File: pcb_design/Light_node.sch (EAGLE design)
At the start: 42 parts, among them CN3 JSTPH, IC1 ATmega328P, IC2 MIC5225-3.3v, U1 MCP73831T-2ACI/OT, U2 LIS3DHTR, Y1 12MHz

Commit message: most of the layour is completed using standard LEDs, but we should move to neopixels on board
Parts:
- removed B2: red, microbuilder:LED0805_NOOUTLINE
- removed C6: 0.1uF, microbuilder:CAP_CERAMIC0805_10MGAP
- removed D2: SCHOTTKY, adafruit:DIODE_SOD-123FL
- removed JP1, JP4: (no value), adafruit:PINHD-1X12-CB
- removed JP6: (no value), microbuilder:HEADER-1X3ROUND
- removed R10: 470 (0603), microbuilder:RESISTOR_0603_NOOUT
- removed U$1, U$6: FIDUCIAL, adafruit:FIDUCIAL
- added CH_LED: GREEN, microbuilder:LED0805_NOOUTLINE
- added LED1: RGB_LED, 0_Shibbs1:RGB_LED
- added LED3, LED4: WS2812B5050, microbuilder:WS2812B5050
- added R13, R14, R15, R17, R18, R9: 470 (0603), microbuilder:RESISTOR_0603_NOOUT
- JP2: device microbuilder:HEADER-1X870MIL -> adafruit:PINHD-1X12-CB
- LED2: value GREEN -> RGB_LED; device microbuilder:LED0805_NOOUTLINE -> 0_Shibbs1:RGB_LED
- renumbered PWR to PWR_LED
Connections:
- removed net VBUS: FTDI.3, JP1.3
- removed net VIN: JP2.1
- new net +5V1: LED3.VDD, LED4.VDD
- new net GND1: LED3.GND, LED4.GND
- new net LED_CNTRL: LED3.DI
- new net N$10: LED2B_LED.-, R14.2
- new net N$11: LED1R_LED.-, R15.2
- new net N$12: LED1G_LED.-, R17.2
- new net N$13: LED1B_LED.-, R18.2
- new net N$14: LED2R_LED.-, R9.2
- new net N$15: LED4.DO
- net +3V3: no longer JP1.4
- net +5V: now also C1.1, D3.C, FTDI.3, IC2.EN, IC2.VIN; no longer D2.A, R10.2
- net 3.3V: no longer C6.1, JP2.2
- net A0: no longer JP4.7
- net A1: no longer JP4.8
- net A2: no longer JP4.9
- net A3: no longer JP4.10
- net A6: no longer R7.WIPER
- net A7: now also R7.WIPER
- net ADC1: no longer JP6.1
- net ADC2: no longer JP6.2
- net ADC3: no longer JP6.3
- net AREF: no longer JP4.6
- net CS: no longer JP2.7
- net D10: now also R9.1; no longer JP4.2
- net D11: now also R13.1; no longer JP4.3
- net D12: now also R14.1; no longer JP4.4
- net D13: no longer JP4.5
- net D2: now also R15.1
- net D3: now also R17.1; no longer JP1.9
- net D4: now also R18.1; no longer JP1.8
- net D5: no longer JP1.7
- net D6: no longer JP1.6
- net D8: no longer JP1.5
- net D9: no longer JP4.1
- net GND: now also CH_LED.C; no longer B2.C, C6.2, JP1.2, JP2.3, LED2.C
- net INT1: no longer JP2.8
- net N$4: now also LED3.DO, LED4.DI; no longer B2.A, R10.1
- net N$7: now also LED2G_LED.-, R13.2; no longer C1.1, D2.C, D3.C, IC2.EN, IC2.VIN
- net N$9: now also CH_LED.A; no longer LED2.A
- net RESET: no longer JP1.12
- net RXD: no longer JP1.11
- net SCL: no longer JP2.4, JP4.12
- net SDA: no longer JP2.5, JP4.11
- net SDO: no longer JP2.6
- net TXD: no longer JP1.10
- net VBAT: now also LED1B_LED.+, LED1G_LED.+, LED1R_LED.+, LED2B_LED.+, LED2G_LED.+, LED2R_LED.+; no longer JP1.1
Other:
- note added: "For USB-powered Designs : Short JP5 and DNP the lithium battery. If you don't do this things are going to get fucked up"
- note removed: "SDA (Pin 6) = Data In (MOSI)"
- note removed: "SDO (Pin 7) = Data Out (MISO)"
- note removed: "SPI"
- note removed: "Set SJ1 to make I2C"
- note removed: "address LSB 1"
- moved on the sheet: C7, CN1, R16, R8, U2

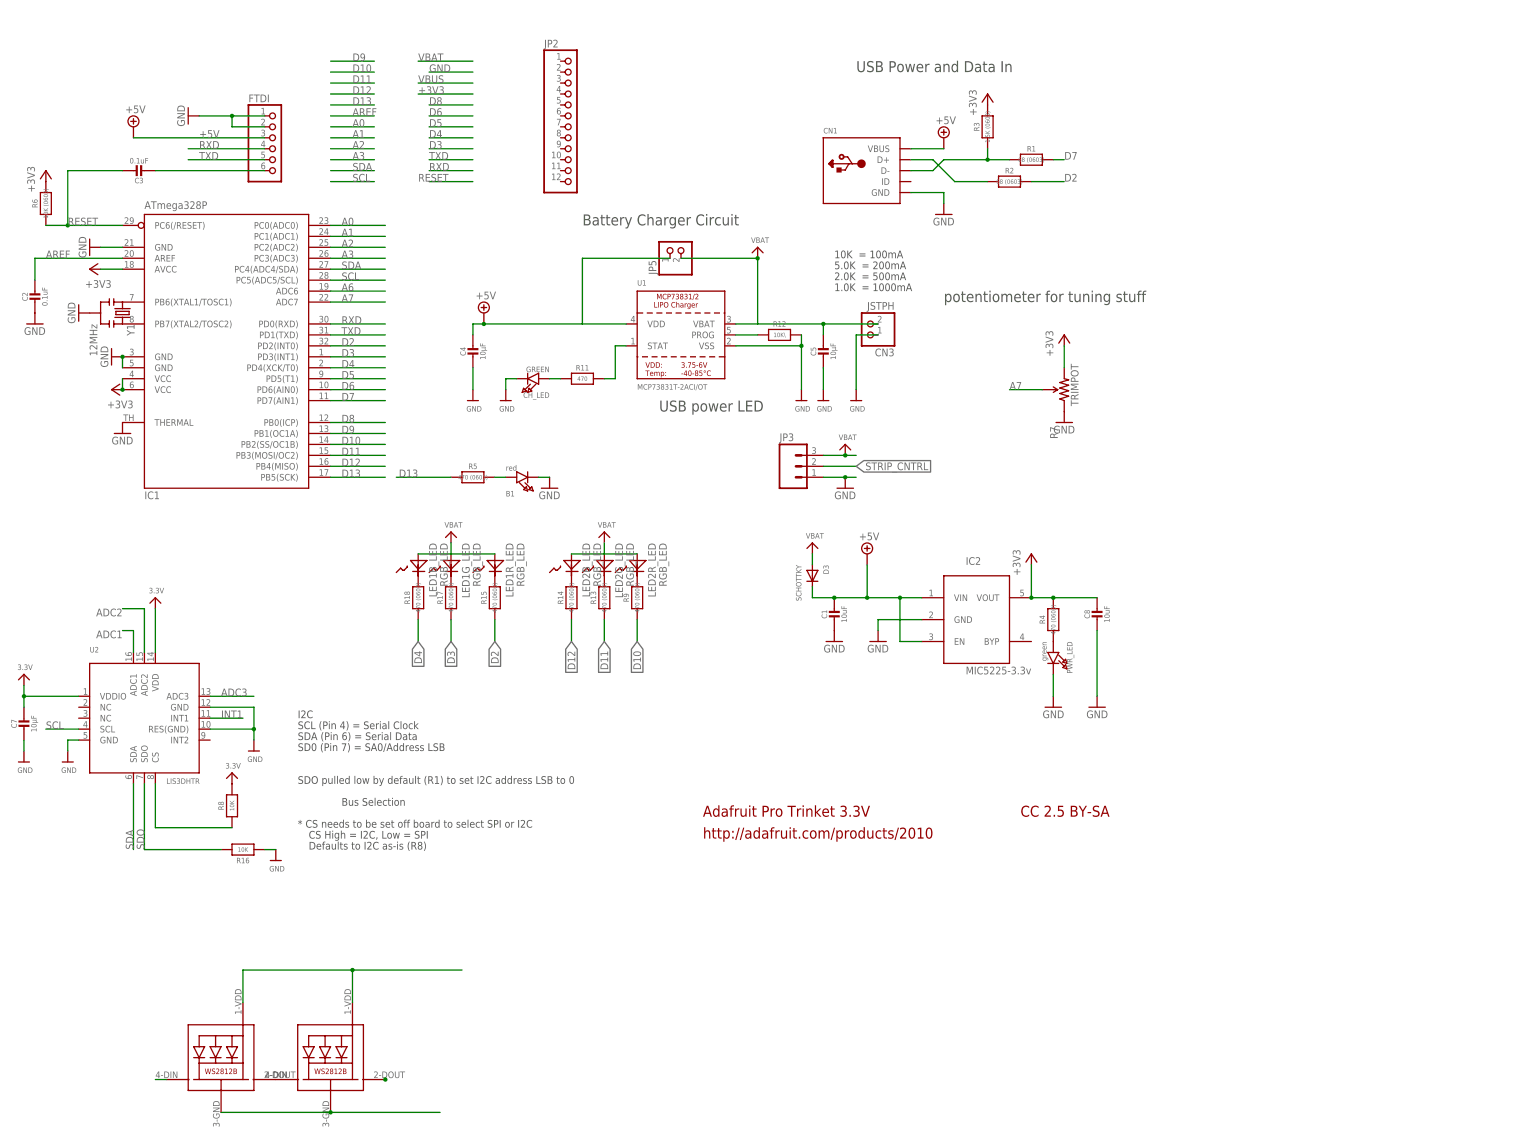
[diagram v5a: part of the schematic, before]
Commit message: moved us to neopixels, added breakout headers, almost done
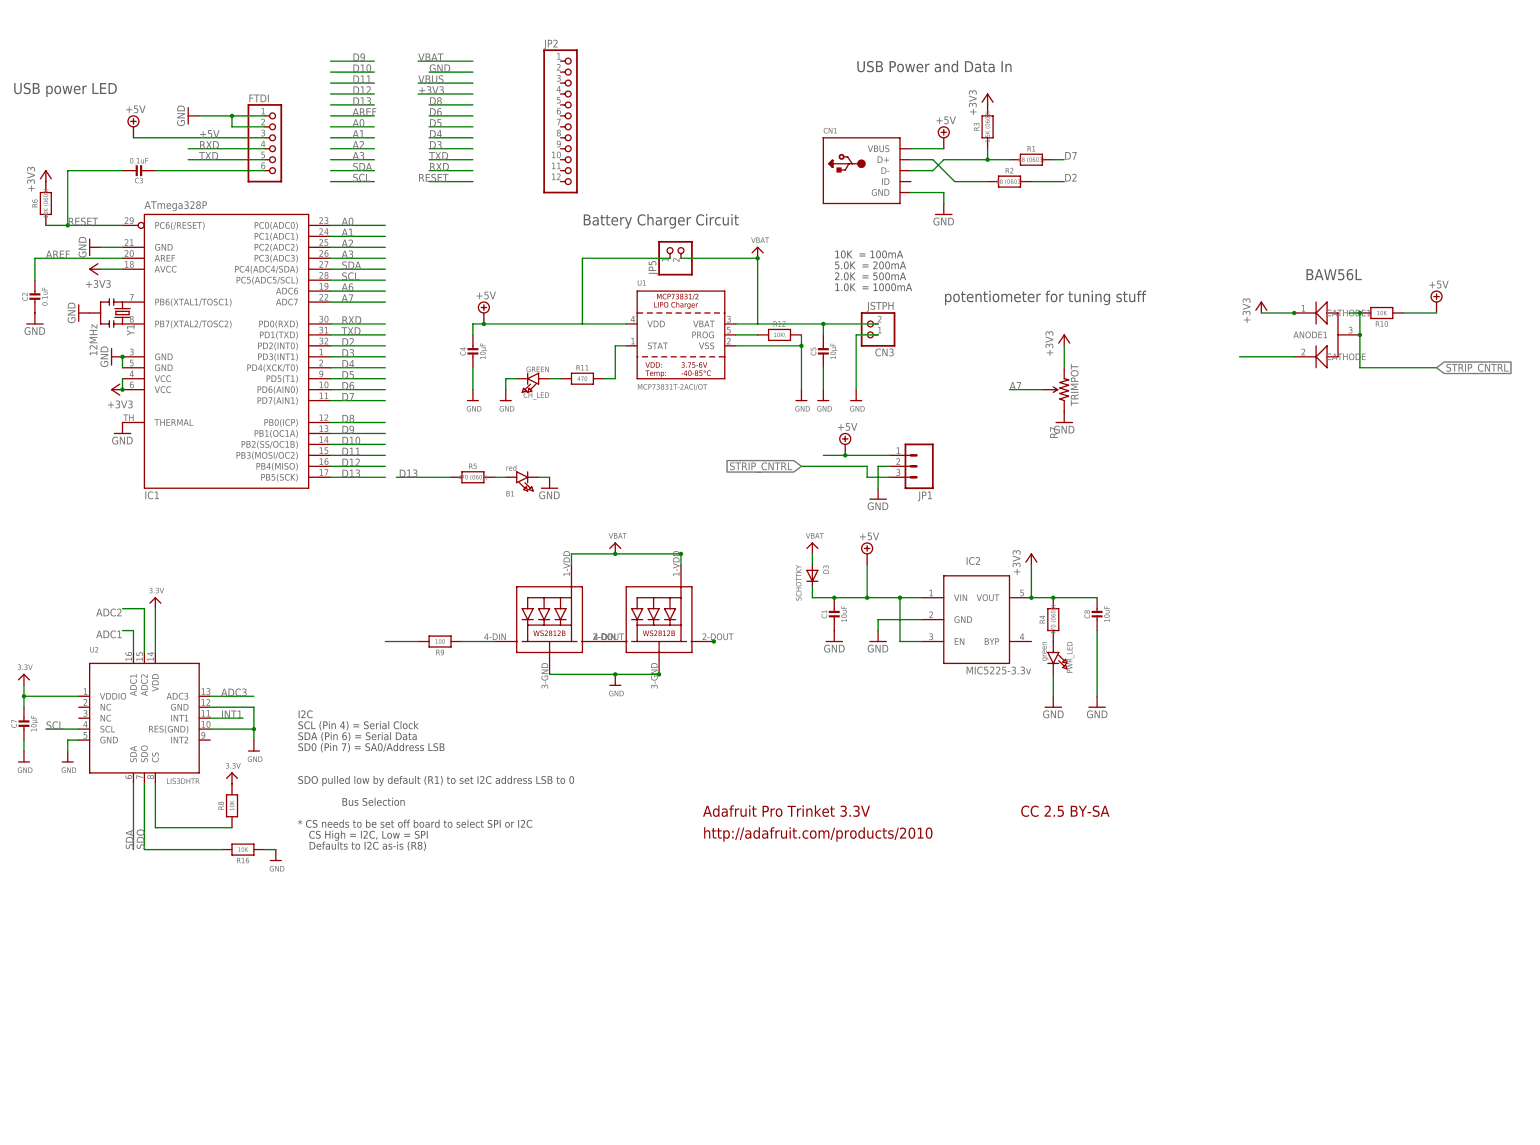
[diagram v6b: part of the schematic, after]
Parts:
- removed JP3: (no value), SparkFun:M03JST-PTH
- removed LED1, LED2: RGB_LED, 0_Shibbs1:RGB_LED
- removed R13, R14, R15, R17, R18: 470 (0603), microbuilder:RESISTOR_0603_NOOUT
- added JP1: (no value), SparkFun:M03JST-PTH
- added R10: 10K, microbuilder:RESISTOR_0603_NOOUT
- added U$9: COMMON_ANODE_DIODE, 0_AlpineLabs:COMMON_ANODE_DIODE
- R9: value 470 (0603) -> 100
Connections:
- removed net +5V1: LED3.VDD, LED4.VDD
- removed net GND1: LED3.GND, LED4.GND
- removed net N$10: LED2B_LED.-, R14.2
- removed net N$11: LED1R_LED.-, R15.2
- removed net N$12: LED1G_LED.-, R17.2
- removed net N$13: LED1B_LED.-, R18.2
- removed net N$14: LED2R_LED.-, R9.2
- removed net N$7: LED2G_LED.-, R13.2
- net +3V3: now also U$9.CATHODE1
- net +5V: now also JP1.1, R10.1
- net D10: now also R9.2; no longer R9.1
- net D11: no longer R13.1
- net D12: no longer R14.1
- net D2: no longer R15.1
- net D3: no longer R17.1
- net D4: now also U$9.CATHODE; no longer R18.1
- net GND: now also JP1.2, LED3.GND, LED4.GND; no longer JP3.1
- net LED_CNTRL: now also R9.1
- net STRIP_CNTRL: now also JP1.3, R10.2, U$9.ANODE1; no longer JP3.2
- net VBAT: now also LED3.VDD, LED4.VDD; no longer JP3.3, LED1B_LED.+, LED1G_LED.+, LED1R_LED.+, LED2B_LED.+, LED2G_LED.+, LED2R_LED.+
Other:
- note added: "BAW56L"
- moved on the sheet: R9

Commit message: Things are pretty close to complete
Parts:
- removed CN1: (no value), microbuilder:USBMICRO_20329
- removed R12: 10K\, microbuilder:RESISTOR0805_NOOUTLINE
- removed R7: TRIMPOT, SparkFun:TRIMPOT
- removed U$9: COMMON_ANODE_DIODE, 0_AlpineLabs:COMMON_ANODE_DIODE
- added JP11: (no value), microbuilder:HEADER-1X2ROUND
- added POT: (no value), 0_Shibbs1:POT
- added R50: 10K, microbuilder:RESISTOR_0603_NOOUT
- added U50: COMMON_ANODE_DIODE, 0_AlpineLabs:COMMON_ANODE_DIODE
- JP1: value (none) -> USB_MICROB_PLUG_CUSTOM; device SparkFun:M03JST-PTH -> 0_AlpineLabs:USB_MICROB_PLUG_CUSTOM
- JP5: value (none) -> M03; device microbuilder:HEADER-1X2ROUND -> 0_Shibbs1:M03
- R10: value 10K -> 470; device microbuilder:RESISTOR_0603_NOOUT -> microbuilder:RESISTOR0805_NOOUTLINE
- R11: value 470 -> 10K\
- renumbered C1 to C40, C2 to C30, C3 to C31, C4 to C10, C5 to C11, C7 to C20, C8 to C41, CN3 to JP3, D3 to D40, IC1 to U30, IC2 to U40, LED3 to RGB1, LED4 to RGB2, R16 to R21, R4 to R40, R6 to R30, R8 to R20, U1 to U10, U2 to U20, Y1 to Y30
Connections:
- removed net 3.3V: C20.1, R20.2, U20.VDD, U20.VDDIO
- removed net INT1: U20.INT1
- net +3V3: now also C20.1, JP2.10, POT.A, R20.2, U20.VDD, U20.VDDIO, U50.CATHODE1; no longer R7.CW, U$9.CATHODE1
- net +5V: now also JP1.VCC, JP11.1, JP2.11, JP5.P$1, R50.1; no longer CN1.VBUS, JP1.1, JP5.1, R10.1
- net A1: now also JP2.2
- net A2: now also JP2.1, U20.INT1
- net A6: now also JP2.3
- net A7: now also POT.S; no longer R7.WIPER
- net D+: now also JP1.D+; no longer CN1.D+
- net D-: now also JP1.D-; no longer CN1.D-
- net D11: now also JP2.7
- net D12: now also JP2.8
- net D3: now also JP2.4
- net D4: now also U50.CATHODE; no longer U$9.CATHODE
- net D5: now also JP2.5
- net D6: now also JP2.6
- net GND: now also JP1.GND, JP2.12, JP5.P$2, POT.E, R11.2; no longer CN1.GND, JP1.2, R12.2, R7.CCW
- net N$5: now also R10.2; no longer R11.2
- net N$8: now also R11.1; no longer R12.1
- net N$9: now also R10.1; no longer R11.1
- net STRIP_CNTRL: now also JP5.P$3, R50.2, U50.ANODE1; no longer JP1.3, R10.2, U$9.ANODE1
- net VBAT: now also JP11.2, JP2.9; no longer JP5.2
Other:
- moved on the sheet: R10, R11
